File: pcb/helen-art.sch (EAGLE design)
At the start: 29 parts, among them IC1 TINY22S, IC2 MCP73811/2

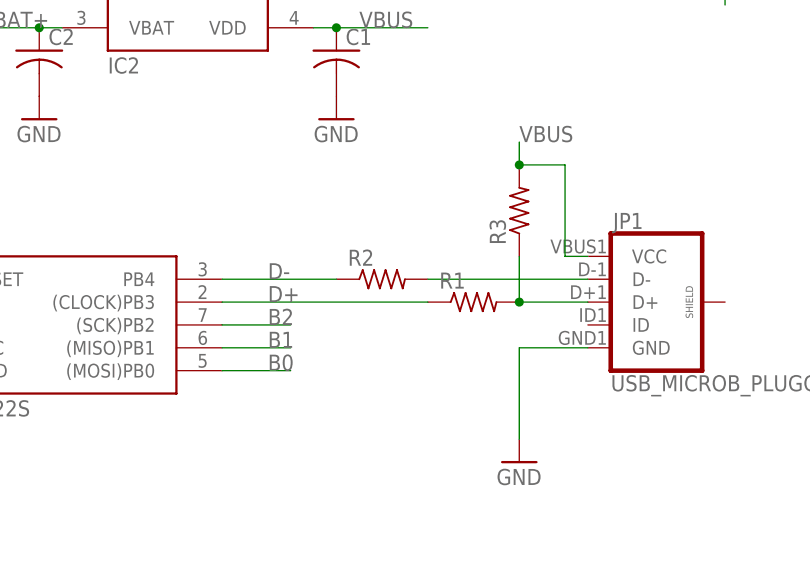
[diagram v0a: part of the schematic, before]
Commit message: fix D+/D- swap and remove LED labels
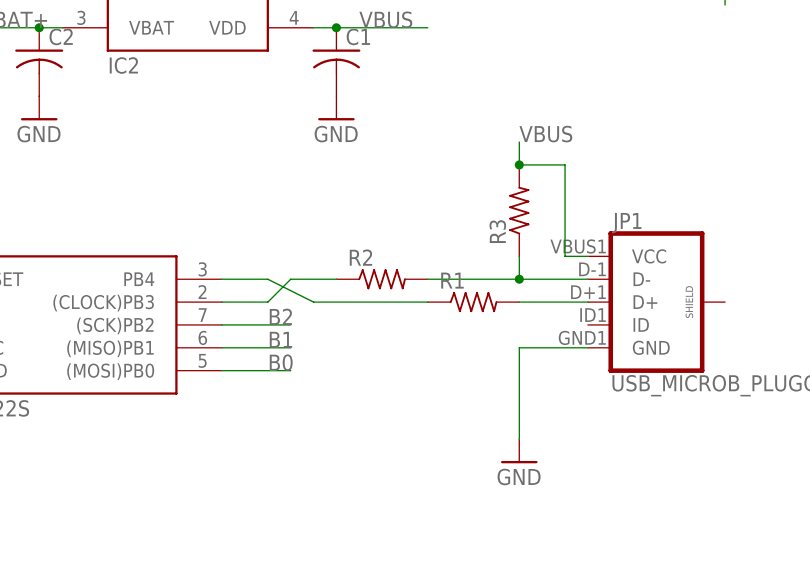
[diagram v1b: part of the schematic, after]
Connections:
- removed net D+: IC1.(CLOCK)PB3, R1.1
- removed net D-: IC1.PB4, R2.1
- new net N$3: IC1.PB4, R1.1
- new net N$4: IC1.(CLOCK)PB3, R2.1
- net N$1: no longer R3.1
- net N$2: now also R3.1
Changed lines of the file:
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@@
 <segment>
 <pinref part="R1" gate="G$1" pin="2"/>
-<pinref part="R3" gate="G$1" pin="1"/>
-<wire x1="124.46" y1="68.58" x2="124.46" y2="63.5" width="0.1524" layer="91"/>
 <wire x1="132.08" y1="63.5" x2="124.46" y2="63.5" width="0.1524" layer="91"/>
 <pinref part="JP1" gate="G$1" pin="D+"/>
-<junction x="124.46" y="63.5"/>
-</segment>
-</net>
-<net name="D+" class="0">
-<segment>
-<pinref part="R1" gate="G$1" pin="1"/>
-<pinref part="IC1" gate="G$1" pin="(CLOCK)PB3"/>
-<wire x1="91.44" y1="63.5" x2="114.3" y2="63.5" width="0.1524" layer="91"/>
-<label x="96.52" y="63.5" size="1.778" layer="95"/>
-</segment>
-</net>
-<net name="D-" class="0">
-<segment>
-<pinref part="IC1" gate="G$1" pin="PB4"/>
-<wire x1="91.44" y1="66.04" x2="104.14" y2="66.04" width="0.1524" layer="91"/>
-<pinref part="R2" gate="G$1" pin="1"/>
-<label x="96.52" y="66.04" size="1.778" layer="95"/>
 </segment>
 </net>
@@
 <segment>
 <pinref part="R2" gate="G$1" pin="2"/>
-<wire x1="114.3" y1="66.04" x2="132.08" y2="66.04" width="0.1524" layer="91"/>
+<wire x1="114.3" y1="66.04" x2="124.46" y2="66.04" width="0.1524" layer="91"/>
 <pinref part="JP1" gate="G$1" pin="D-"/>
+<pinref part="R3" gate="G$1" pin="1"/>
+<wire x1="124.46" y1="66.04" x2="132.08" y2="66.04" width="0.1524" layer="91"/>
+<wire x1="124.46" y1="66.04" x2="124.46" y2="68.58" width="0.1524" layer="91"/>
+<junction x="124.46" y="66.04"/>
 </segment>
 </net>
@@
 </segment>
 </net>
+<net name="N$3" class="0">
+<segment>
+<pinref part="R1" gate="G$1" pin="1"/>
+<wire x1="114.3" y1="63.5" x2="101.6" y2="63.5" width="0.1524" layer="91"/>
+<wire x1="101.6" y1="63.5" x2="96.52" y2="66.04" width="0.1524" layer="91"/>
+<pinref part="IC1" gate="G$1" pin="PB4"/>
+<wire x1="96.52" y1="66.04" x2="91.44" y2="66.04" width="0.1524" layer="91"/>
+</segment>
+</net>
+<net name="N$4" class="0">
+<segment>
+<pinref part="IC1" gate="G$1" pin="(CLOCK)PB3"/>
+<wire x1="91.44" y1="63.5" x2="96.52" y2="63.5" width="0.1524" layer="91"/>
+<wire x1="96.52" y1="63.5" x2="99.06" y2="66.04" width="0.1524" layer="91"/>
+<pinref part="R2" gate="G$1" pin="1"/>
+<wire x1="99.06" y1="66.04" x2="104.14" y2="66.04" width="0.1524" layer="91"/>
+</segment>
+</net>

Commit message: values for resistors
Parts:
- R1, R2: value (none) -> 68
- R3: value (none) -> 1.0k
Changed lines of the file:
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@@
 <parts>
 <part name="IC1" library="atmel" deviceset="TINY22" device="S"/>
-<part name="R1" library="resistor" deviceset="R-US_" device="R0603"/>
-<part name="R2" library="resistor" deviceset="R-US_" device="R0603"/>
-<part name="R3" library="resistor" deviceset="R-US_" device="R0603"/>
+<part name="R1" library="resistor" deviceset="R-US_" device="R0603" value="68"/>
+<part name="R2" library="resistor" deviceset="R-US_" device="R0603" value="68"/>
+<part name="R3" library="resistor" deviceset="R-US_" device="R0603" value="1.0k"/>
 <part name="GND1" library="supply1" deviceset="GND" device=""/>
 <part name="GND8" library="supply1" deviceset="GND" device=""/>
